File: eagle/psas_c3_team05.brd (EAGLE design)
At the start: 100 x 71.1 mm, 81 parts, among them IC1 CP2102, Q1 32 MHz, U1 MIC5219 3.3V, U2 MCP73871

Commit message: Finished power traces (I think)
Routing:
- net 3.3V: track 132.5 -> 250.7 mm, vias 3 -> 10
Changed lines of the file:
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@@
 <via x="65.1002" y="11.7602" extent="1-16" drill="0.3302"/>
 <via x="89.9414" y="16.1544" extent="1-16" drill="0.3302"/>
-<via x="71.628" y="50.292" extent="1-16" drill="0.3302"/>
+<via x="73.9902" y="52.0954" extent="1-16" drill="0.3302"/>
 <via x="69.342" y="51.816" extent="1-16" drill="0.3302"/>
 <via x="67.564" y="50.8" extent="1-16" drill="0.3302"/>
@@
 <wire x1="64.178175" y1="33.9598" x2="64.178175" y2="33.7184" width="0.254" layer="1"/>
 <wire x1="9.855096875" y1="56.2991" x2="4.5546" y2="54.00341875" width="0" layer="19" extent="1-1"/>
+<wire x1="72.909521875" y1="36.4784" x2="77.724" y2="36.6394" width="0" layer="19" extent="1-1"/>
+<wire x1="72.909521875" y1="35.4784" x2="72.909521875" y2="36.4784" width="0" layer="19" extent="1-1"/>
 </signal>
 <signal name="VOUT">
@@
 <wire x1="68.1482" y1="41.8338" x2="67.934521875" y2="41.620121875" width="0.254" layer="1"/>
 <wire x1="67.934521875" y1="41.620121875" x2="67.934521875" y2="40.4534" width="0.254" layer="1"/>
-<wire x1="78.359" y1="27.94" x2="80.350359375" y2="27.94" width="0.762" layer="1"/>
 <wire x1="80.350359375" y1="27.94" x2="80.350359375" y2="27.9424375" width="0.254" layer="1"/>
 <wire x1="72.909521875" y1="36.9784" x2="76.9874" y2="36.9784" width="0.254" layer="1"/>
@@
 <wire x1="44.9682625" y1="58.087165625" x2="45.839384375" y2="57.21604375" width="0.762" layer="1"/>
 <wire x1="78.02635625" y1="38.2778" x2="79.695140625" y2="39.946584375" width="0.762" layer="1"/>
-<wire x1="79.695140625" y1="39.946584375" x2="79.695140625" y2="40.302184375" width="0.762" layer="1"/>
-<wire x1="78.359" y1="27.94" x2="78.3082" y2="27.9908" width="0.762" layer="1"/>
-<wire x1="78.3082" y1="27.9908" x2="78.3082" y2="31.1658" width="0.762" layer="1"/>
 <wire x1="72.434521875" y1="33.0034" x2="72.443321875" y2="32.9946" width="0.254" layer="1"/>
-<wire x1="72.443321875" y1="32.9946" x2="78.2828" y2="32.9946" width="0.381" layer="1"/>
-<wire x1="78.2828" y1="32.9946" x2="78.3082" y2="32.9692" width="0.254" layer="1"/>
-<wire x1="78.3082" y1="32.9692" x2="78.3082" y2="31.1658" width="0.381" layer="1"/>
+<wire x1="72.443321875" y1="32.9946" x2="78.3336" y2="32.9946" width="0.381" layer="1"/>
+<wire x1="78.3336" y1="32.9946" x2="78.3336" y2="32.9692" width="0.254" layer="1"/>
+<wire x1="78.3336" y1="32.9692" x2="78.3336" y2="31.1658" width="0.381" layer="1"/>
 <wire x1="64.09436875" y1="30.40624375" x2="60.8584" y2="30.40624375" width="0.762" layer="1"/>
 <wire x1="60.8584" y1="30.40624375" x2="60.8584" y2="23.2918" width="0.762" layer="1"/>
-<wire x1="60.8584" y1="23.2918" x2="58.6232" y2="21.082" width="0.762" layer="1"/>
+<wire x1="60.8584" y1="23.2918" x2="58.83835625" y2="21.2947125" width="0.762" layer="1"/>
+<wire x1="58.83835625" y1="21.2947125" x2="58.6232" y2="21.082" width="0.762" layer="1"/>
 <wire x1="58.6232" y1="21.082" x2="38.8112" y2="21.082" width="0.762" layer="1"/>
 <via x="35.2298" y="17.5768" extent="1-16" drill="0.3302"/>
@@
 <wire x1="35.2298" y1="17.5768" x2="25.747984375" y2="8.094984375" width="0.762" layer="16"/>
 <wire x1="25.747984375" y1="8.094984375" x2="25.747984375" y2="6.7030625" width="0.762" layer="16"/>
+<wire x1="78.3336" y1="31.1658" x2="78.3336" y2="27.7368" width="0.762" layer="1"/>
+<via x="78.3336" y="19.7358" extent="1-16" drill="0.3302"/>
+<wire x1="78.3336" y1="27.7368" x2="78.3336" y2="19.7358" width="0.762" layer="1"/>
+<wire x1="78.3336" y1="19.7358" x2="78.3336" y2="16.3322" width="0.762" layer="16"/>
+<wire x1="78.3336" y1="16.3322" x2="68.9102" y2="6.9088" width="0.762" layer="16"/>
+<via x="68.9102" y="6.9088" extent="1-16" drill="0.3302"/>
+<wire x1="68.9102" y1="6.9088" x2="68.9102" y2="10.795" width="0.762" layer="1"/>
+<wire x1="68.9102" y1="10.795" x2="63.627" y2="16.0782" width="0.762" layer="1"/>
+<via x="63.627" y="16.0782" extent="1-16" drill="0.3302"/>
+<wire x1="63.627" y1="16.0782" x2="58.6232" y2="21.082" width="0.762" layer="16"/>
+<via x="58.6232" y="21.082" extent="1-16" drill="0.3302"/>
+<wire x1="58.6232" y1="21.082" x2="58.62564375" y2="21.082" width="0.4064" layer="1"/>
+<wire x1="58.62564375" y1="21.082" x2="58.83835625" y2="21.2947125" width="0.4064" layer="1"/>
+<wire x1="80.350359375" y1="27.9424375" x2="78.5392375" y2="27.9424375" width="0.762" layer="1"/>
+<wire x1="78.5392375" y1="27.9424375" x2="78.3336" y2="27.7368" width="0.762" layer="1"/>
+<wire x1="79.695140625" y1="40.302184375" x2="79.695140625" y2="40.477540625" width="0.762" layer="1"/>
+<wire x1="79.695140625" y1="40.477540625" x2="87.122" y2="47.9044" width="0.762" layer="1"/>
+<wire x1="87.122" y1="47.9044" x2="95.6564" y2="47.9044" width="0.762" layer="1"/>
+<wire x1="95.6564" y1="47.9044" x2="97.79" y2="50.038" width="0.762" layer="1"/>
+<wire x1="97.79" y1="50.038" x2="97.79" y2="61.3156" width="0.762" layer="1"/>
+<wire x1="97.79" y1="61.3156" x2="95.6564" y2="63.4492" width="0.762" layer="1"/>
+<wire x1="95.6564" y1="63.4492" x2="86.7156" y2="63.4492" width="0.762" layer="1"/>
+<wire x1="86.7156" y1="63.4492" x2="83.8708" y2="60.6044" width="0.762" layer="1"/>
+<via x="83.8708" y="60.6044" extent="1-16" drill="0.3302"/>
+<wire x1="83.8708" y1="60.6044" x2="81.1022" y2="60.6044" width="0.762" layer="16"/>
+<wire x1="81.1022" y1="60.6044" x2="81.0768" y2="60.6298" width="0.762" layer="16"/>
+<via x="81.0768" y="60.6298" extent="1-16" drill="0.3302"/>
+<wire x1="81.0768" y1="60.6298" x2="81.0768" y2="63.246" width="0.762" layer="1"/>
+<via x="81.0768" y="63.246" extent="1-16" drill="0.3302"/>
+<wire x1="81.0768" y1="63.246" x2="79.6544" y2="63.246" width="0.762" layer="16"/>
+<wire x1="79.6544" y1="63.246" x2="71.4248" y2="55.0164" width="0.762" layer="16"/>
+<wire x1="71.4248" y1="55.0164" x2="71.4248" y2="49.4538" width="0.762" layer="16"/>
+<wire x1="71.4248" y1="49.4538" x2="70.5358" y2="48.5648" width="0.762" layer="16"/>
+<wire x1="79.695140625" y1="40.302184375" x2="79.695140625" y2="39.946584375" width="0" layer="19" extent="1-1"/>
 <wire x1="72.434521875" y1="33.0034" x2="72.909521875" y2="36.9784" width="0" layer="19" extent="1-1"/>
-<wire x1="66.434521875" y1="33.0034" x2="72.434521875" y2="33.0034" width="0" layer="19" extent="1-1"/>
-<wire x1="65.934521875" y1="33.0034" x2="66.434521875" y2="33.0034" width="0" layer="19" extent="1-1"/>
-<wire x1="65.459521875" y1="33.4784" x2="65.934521875" y2="33.0034" width="0" layer="19" extent="1-1"/>
-<wire x1="64.178175" y1="32.1184" x2="65.459521875" y2="33.4784" width="0" layer="19" extent="1-1"/>
-<wire x1="64.09436875" y1="30.40624375" x2="64.178175" y2="32.1184" width="0" layer="19" extent="1-1"/>
+<wire x1="64.178175" y1="32.1184" x2="64.09436875" y2="30.40624375" width="0" layer="19" extent="1-1"/>
 <wire x1="65.824103125" y1="30.408778125" x2="64.09436875" y2="30.40624375" width="0" layer="19" extent="1-1"/>
-<wire x1="67.934521875" y1="40.4534" x2="72.909521875" y2="36.9784" width="0" layer="19" extent="1-1"/>
+<wire x1="65.459521875" y1="33.4784" x2="64.178175" y2="32.1184" width="0" layer="19" extent="1-1"/>
+<wire x1="65.934521875" y1="33.0034" x2="65.459521875" y2="33.4784" width="0" layer="19" extent="1-1"/>
+<wire x1="66.434521875" y1="33.0034" x2="65.934521875" y2="33.0034" width="0" layer="19" extent="1-1"/>
 </signal>
 <signal name="VBUS">

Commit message: Changed values for RF
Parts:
- C10: value 10p -> 15p
- C11: value 15p -> 12p
- C16: value 1nF -> 10nF
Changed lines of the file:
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@@
 <elements>
 <element name="C1" library="rcl_custom" package=".0603-B-NOSILK" value="10uF" x="21.01341875" y="46.2813375" rot="R270"/>
-<element name="C10" library="rcl_custom" package=".0603-B-NOSILK" value="10p" x="80.8228" y="35.0266" rot="R180"/>
-<element name="C11" library="rcl_custom" package=".0603-B-NOSILK" value="15p" x="77.724" y="35.8394" rot="R90"/>
+<element name="C10" library="rcl_custom" package=".0603-B-NOSILK" value="15p" x="80.8228" y="35.0266" rot="R180"/>
+<element name="C11" library="rcl_custom" package=".0603-B-NOSILK" value="12p" x="77.724" y="35.8394" rot="R90"/>
 <element name="C12" library="rcl_custom" package=".0603-B-NOSILK" value="2.2p" x="84.4042" y="37.31768125" rot="R180"/>
 <element name="C13" library="rcl_custom" package=".0603-B-NOSILK" value="15p" x="85.2678" y="39.8272" rot="R90"/>
 <element name="C14" library="rcl_custom" package=".0603-B-NOSILK" value="8.2p" x="90.6526" y="35.7886" rot="R90"/>
 <element name="C15" library="rcl_custom" package=".0603-B-NOSILK" value="100nF" x="93.218" y="35.052"/>
-<element name="C16" library="rcl_custom" package=".0603-B-NOSILK" value="1nF" x="82.4001375" y="31.8389" rot="R180"/>
+<element name="C16" library="rcl_custom" package=".0603-B-NOSILK" value="10nF" x="82.4001375" y="31.8389" rot="R180"/>
 <element name="C2" library="rcl_custom" package=".0603-B-NOSILK" value="100nF" x="37.538659375" y="59.0296"/>
 <element name="C3" library="rcl_custom" package=".0603-B-NOSILK" value="4.7uF" x="38.000940625" y="62.209678125" rot="R270"/>

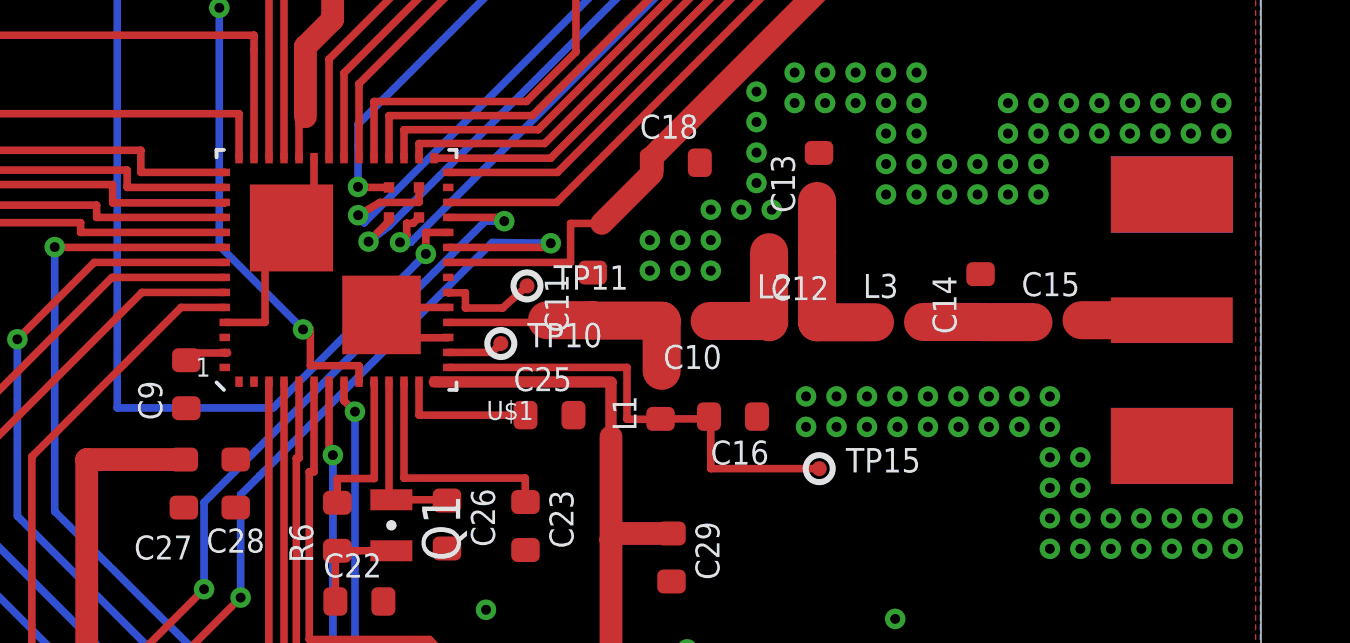
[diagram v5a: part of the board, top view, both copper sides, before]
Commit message: Raised trace width for RF to 0.05in
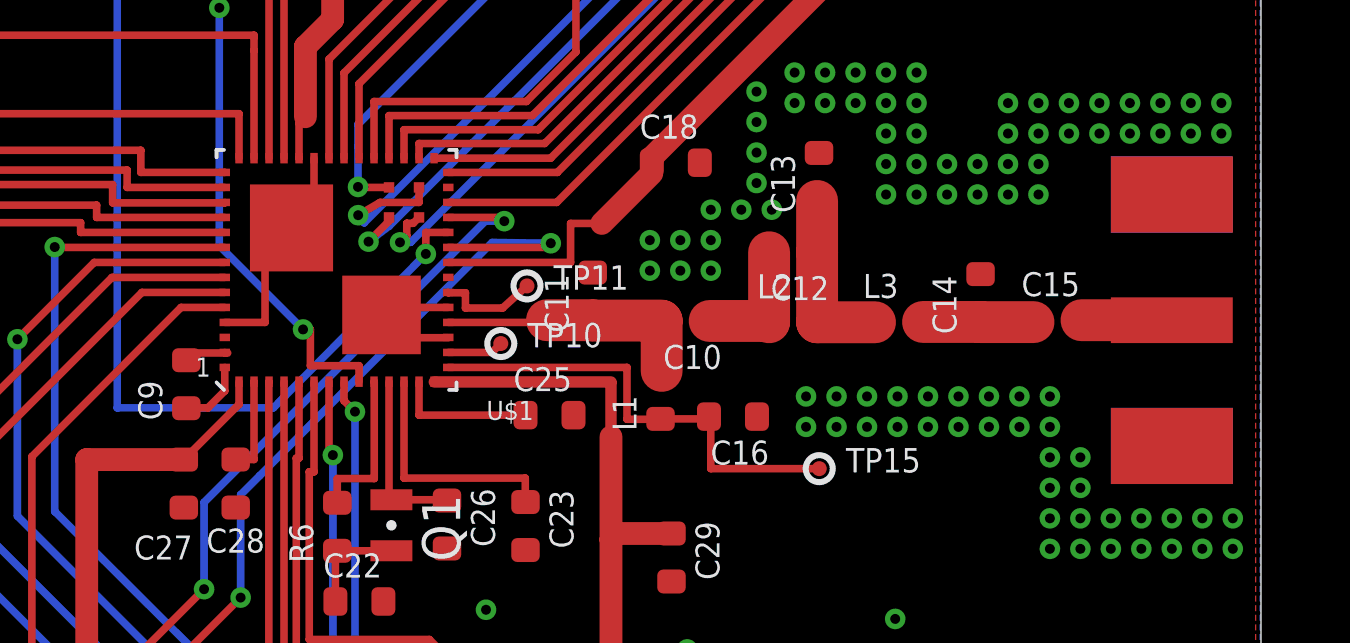
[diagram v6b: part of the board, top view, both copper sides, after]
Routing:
- net 3.3V: track 250.7 -> 259.6 mm
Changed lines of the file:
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@@
 <wire x1="71.4248" y1="55.0164" x2="71.4248" y2="49.4538" width="0.762" layer="16"/>
 <wire x1="71.4248" y1="49.4538" x2="70.5358" y2="48.5648" width="0.762" layer="16"/>
+<wire x1="65.824103125" y1="30.408778125" x2="66.434521875" y2="30.408778125" width="0.254" layer="1"/>
+<wire x1="66.434521875" y1="30.408778125" x2="66.434521875" y2="33.0034" width="0.254" layer="1"/>
+<wire x1="65.934521875" y1="33.0034" x2="65.934521875" y2="32.246396875" width="0.254" layer="1"/>
+<wire x1="65.934521875" y1="32.246396875" x2="64.09436875" y2="30.40624375" width="0.254" layer="1"/>
+<wire x1="65.459521875" y1="33.4784" x2="65.459521875" y2="32.693521875" width="0.254" layer="1"/>
+<wire x1="65.459521875" y1="32.693521875" x2="64.897" y2="32.131" width="0.254" layer="1"/>
+<wire x1="64.897" y1="32.131" x2="64.190775" y2="32.131" width="0.254" layer="1"/>
+<wire x1="64.190775" y1="32.131" x2="64.178175" y2="32.1184" width="0.254" layer="1"/>
 <wire x1="79.695140625" y1="40.302184375" x2="79.695140625" y2="39.946584375" width="0" layer="19" extent="1-1"/>
 <wire x1="72.434521875" y1="33.0034" x2="72.909521875" y2="36.9784" width="0" layer="19" extent="1-1"/>
-<wire x1="64.178175" y1="32.1184" x2="64.09436875" y2="30.40624375" width="0" layer="19" extent="1-1"/>
-<wire x1="65.824103125" y1="30.408778125" x2="64.09436875" y2="30.40624375" width="0" layer="19" extent="1-1"/>
-<wire x1="65.459521875" y1="33.4784" x2="64.178175" y2="32.1184" width="0" layer="19" extent="1-1"/>
-<wire x1="65.934521875" y1="33.0034" x2="65.459521875" y2="33.4784" width="0" layer="19" extent="1-1"/>
 <wire x1="66.434521875" y1="33.0034" x2="65.934521875" y2="33.0034" width="0" layer="19" extent="1-1"/>
+<wire x1="65.459521875" y1="32.693521875" x2="65.934521875" y2="33.0034" width="0" layer="19" extent="1-1"/>
 </signal>
 <signal name="VBUS">
@@
 <wire x1="72.909521875" y1="34.9784" x2="76.2" y2="34.9784" width="0.254" layer="1"/>
 <wire x1="76.2" y1="34.9784" x2="76.2" y2="35.052" width="1.016" layer="1"/>
-<wire x1="76.2" y1="35.052" x2="77.724" y2="35.052" width="1.27" layer="1"/>
+<wire x1="76.2" y1="35.052" x2="77.724" y2="35.052" width="1.397" layer="1"/>
 <wire x1="77.724" y1="35.052" x2="77.724" y2="35.0394" width="1.016" layer="1"/>
-<wire x1="77.724" y1="35.0394" x2="80.0228" y2="35.0394" width="1.27" layer="1"/>
+<wire x1="77.724" y1="35.0394" x2="80.0228" y2="35.0394" width="1.397" layer="1"/>
 <wire x1="80.0228" y1="35.0394" x2="80.0228" y2="35.0266" width="1.016" layer="1"/>
 <wire x1="79.9846" y1="33.3628" x2="80.0228" y2="33.3628" width="1.016" layer="1"/>
-<wire x1="80.0228" y1="33.3628" x2="80.0228" y2="35.0266" width="1.27" layer="1"/>
+<wire x1="80.0228" y1="33.3628" x2="80.0228" y2="35.0266" width="1.397" layer="1"/>
 </signal>
 <signal name="N$17">
@@
 <contactref element="L2" pad="2"/>
 <contactref element="L3" pad="1"/>
-<wire x1="85.2042" y1="34.98341875" x2="87.1348" y2="34.98341875" width="1.27" layer="1"/>
+<wire x1="85.2042" y1="34.98341875" x2="87.1348" y2="34.98341875" width="1.397" layer="1"/>
 <wire x1="87.1348" y1="34.98341875" x2="87.1348" y2="34.993578125" width="1.016" layer="1"/>
-<wire x1="85.2042" y1="37.31768125" x2="85.2042" y2="34.98341875" width="1.27" layer="1"/>
+<wire x1="85.2042" y1="37.31768125" x2="85.2042" y2="34.98341875" width="1.397" layer="1"/>
 <wire x1="85.2678" y1="39.0272" x2="85.2042" y2="39.0272" width="1.016" layer="1"/>
-<wire x1="85.2042" y1="39.0272" x2="85.2042" y2="37.31768125" width="1.27" layer="1"/>
+<wire x1="85.2042" y1="39.0272" x2="85.2042" y2="37.31768125" width="1.397" layer="1"/>
 </signal>
 <signal name="N$18">
@@
 <contactref element="C12" pad="2"/>
 <contactref element="L2" pad="1"/>
-<wire x1="81.6228" y1="35.0266" x2="83.6042" y2="35.0266" width="1.27" layer="1"/>
+<wire x1="81.6228" y1="35.0266" x2="83.6042" y2="35.0266" width="1.397" layer="1"/>
 <wire x1="83.6042" y1="35.0266" x2="83.6042" y2="34.98341875" width="1.016" layer="1"/>
-<wire x1="83.6042" y1="34.98341875" x2="83.6042" y2="37.31768125" width="1.27" layer="1"/>
+<wire x1="83.6042" y1="34.98341875" x2="83.6042" y2="37.31768125" width="1.397" layer="1"/>
 </signal>
 <signal name="N$19">
 <contactref element="C15" pad="2"/>
 <contactref element="U$2" pad="P$3"/>
-<wire x1="94.018" y1="35.052" x2="97.028" y2="35.052" width="1.27" layer="1"/>
+<wire x1="94.018" y1="35.052" x2="97.028" y2="35.052" width="1.397" layer="1"/>
 </signal>
 <signal name="VR_PA">
@@
 <contactref element="C15" pad="1"/>
 <contactref element="L3" pad="2"/>
-<wire x1="88.7348" y1="34.993578125" x2="90.6526" y2="34.993578125" width="1.27" layer="1"/>
+<wire x1="88.7348" y1="34.993578125" x2="90.6526" y2="34.993578125" width="1.397" layer="1"/>
 <wire x1="90.6526" y1="34.993578125" x2="90.6526" y2="34.9886" width="1.016" layer="1"/>
-<wire x1="90.6526" y1="34.9886" x2="92.418" y2="34.9886" width="1.27" layer="1"/>
+<wire x1="90.6526" y1="34.9886" x2="92.418" y2="34.9886" width="1.397" layer="1"/>
 <wire x1="92.418" y1="34.9886" x2="92.418" y2="35.052" width="1.016" layer="1"/>
 </signal>

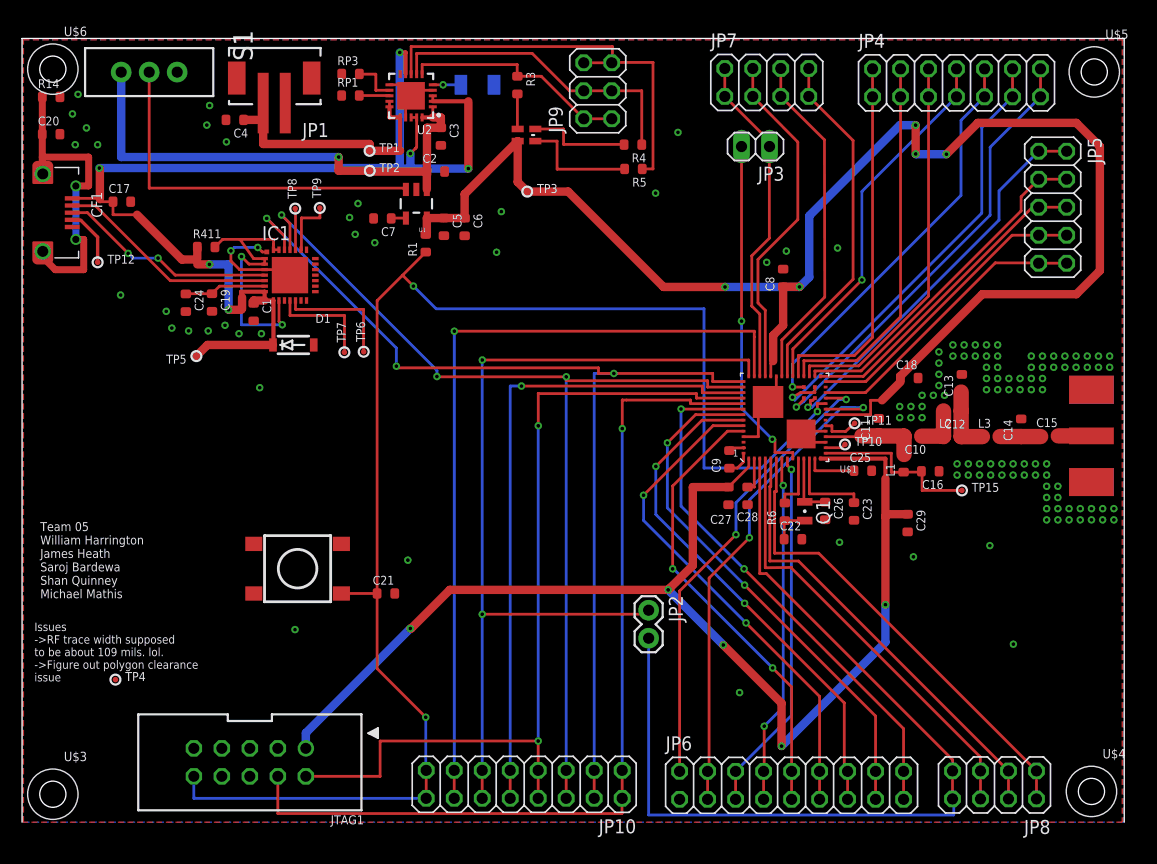
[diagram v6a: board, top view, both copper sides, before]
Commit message: Adjusted the position of labels, and added missing boader
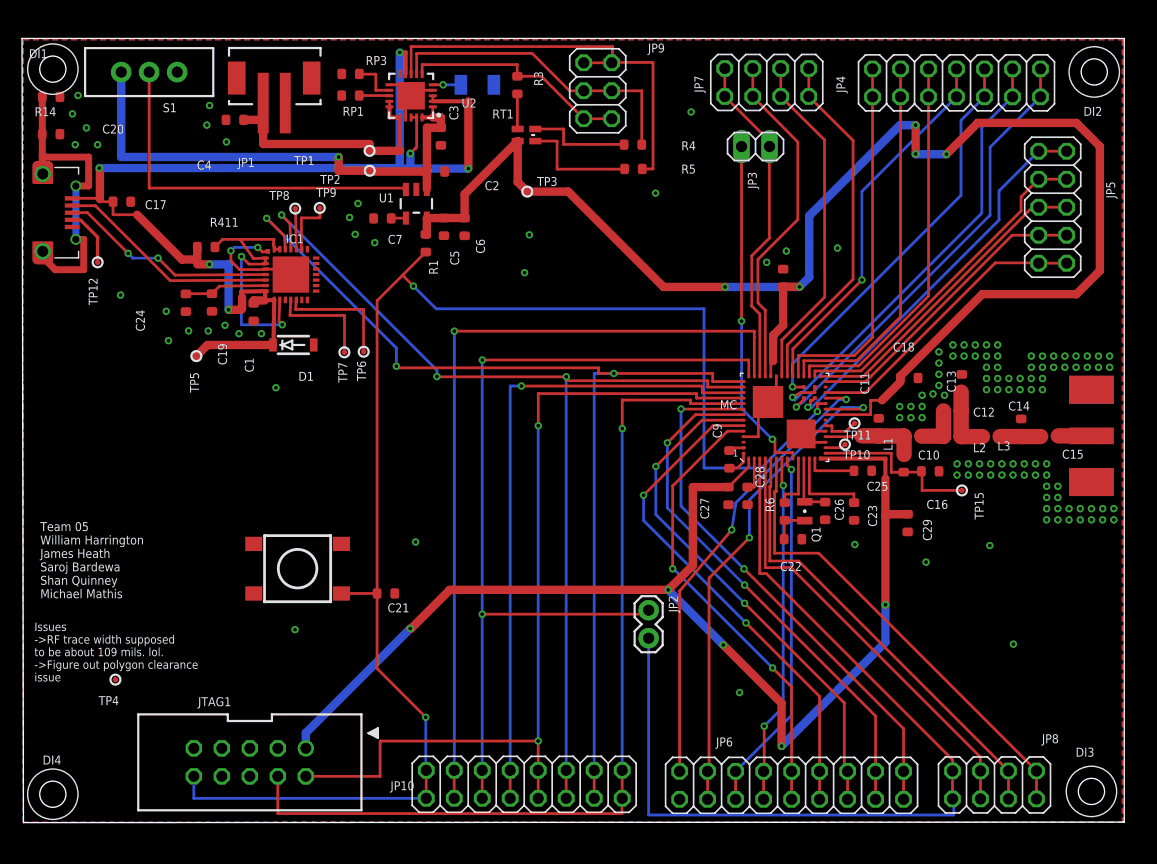
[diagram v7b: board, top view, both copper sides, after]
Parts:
- JP1: value battery_connector -> BC
- moved IC1 0.09 mm to (24.4, 49.7)
- renumbered U$1 to MC, U$3 to DI4, U$4 to DI3, U$5 to DI2, U$6 to DI1
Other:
- board size 100 x 71.1 mm -> 100 x 71.2 mm
